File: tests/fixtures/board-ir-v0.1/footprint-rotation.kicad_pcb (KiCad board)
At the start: 2 copper layers, 44 x 40 mm, 8 parts

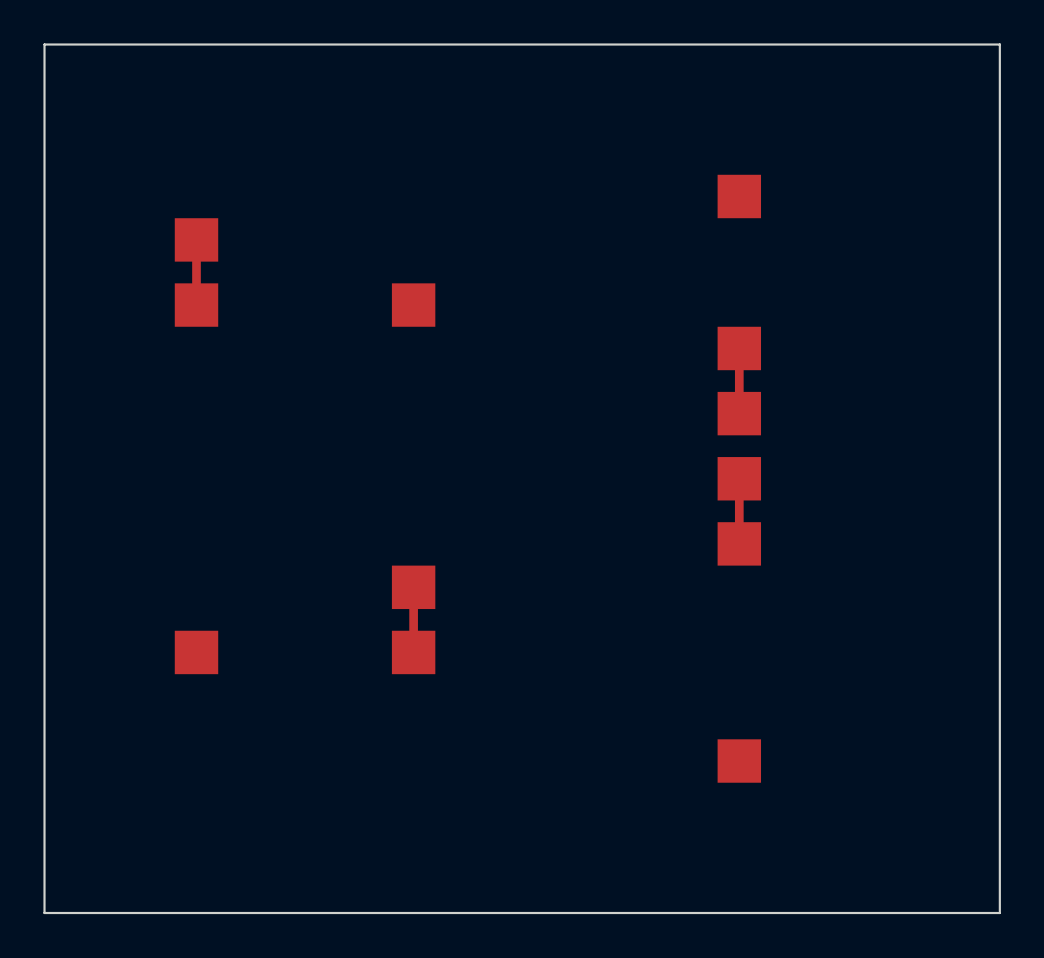
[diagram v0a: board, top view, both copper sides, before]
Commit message: fix: rotate pads absolutely and close six scene observation gaps (#41)
KiCad pad angles are absolute in the board frame, so the adapter's
addition of the footprint rotation double-counted every rotated pad and
transposed extents on non-square pads; the fix is pinned by the first
adapter test adjudicated by an external oracle, comparing Board IR
extents against the geometry KiCad itself plots, mutation-tested by
reinstating the defect. On the reference board different-net bbox
overlaps fall from six to one, the survivor being a corner both real
shapes round away, and no route outcome changes. The scene closes its
review findings: annotations are budgeted with explicit truncation,
region bounds include the arc extrema a sweep actually crosses under a
magnitude-independent exact comparator verified over four hundred
random arcs, oblique pads fall back to the circumscribed circle rather
than under-bounding, locked copper carries a per-object flag while the
partition stays exhaustive by kind, roundrect corner radii reach the
contract, and around-reference radii clamp losslessly instead of
overflowing. Golden fixture changes are exactly two pad rotations plus
the digest, diffed field by field before regeneration.

Co-authored-by: Seung Hyuk Choe <10142803+seunghyukchoe@users.noreply.github.com>
Co-authored-by: Claude Fable 5 <noreply@anthropic.com>
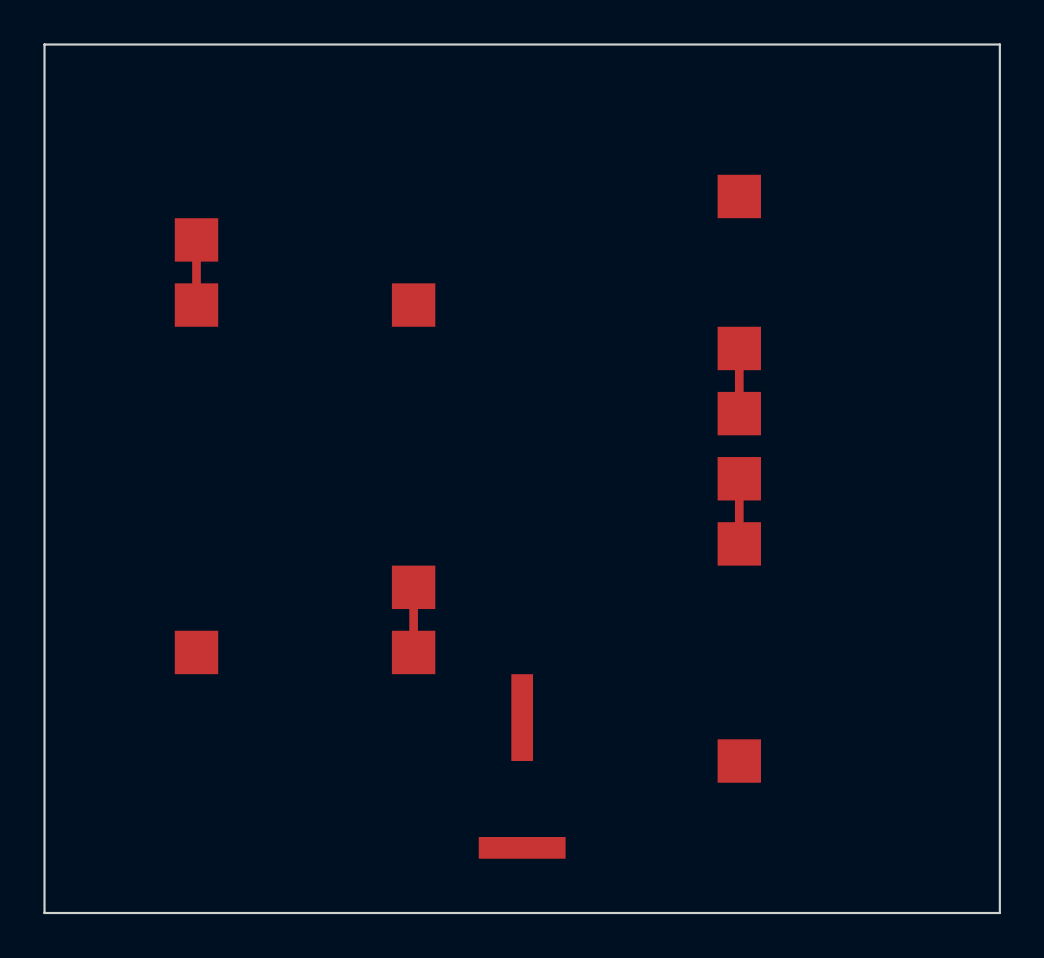
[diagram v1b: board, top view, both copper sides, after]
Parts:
- added ?: , RotationOblong_90, F.Cu at (22.0, 34.0)
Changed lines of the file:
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@@
     (at 32 12 90)
     (pad "1" smd rect
-      (at -5 0)
+      (at -5 0 90)
       (size 2 2)
       (layers "F.Cu" "F.Mask" "F.Paste")
@@
     )
     (pad "2" smd rect
-      (at 5 0)
+      (at 5 0 90)
       (size 2 2)
       (layers "F.Cu" "F.Mask" "F.Paste")
@@
     (at 12 28 180)
     (pad "1" smd rect
-      (at -5 0)
+      (at -5 0 180)
       (size 2 2)
       (layers "F.Cu" "F.Mask" "F.Paste")
@@
     )
     (pad "2" smd rect
-      (at 5 0)
+      (at 5 0 180)
       (size 2 2)
       (layers "F.Cu" "F.Mask" "F.Paste")
@@
     (at 32 28 270)
     (pad "1" smd rect
-      (at -5 0)
+      (at -5 0 270)
       (size 2 2)
       (layers "F.Cu" "F.Mask" "F.Paste")
@@
     )
     (pad "2" smd rect
-      (at 5 0)
+      (at 5 0 270)
       (size 2 2)
       (layers "F.Cu" "F.Mask" "F.Paste")
@@
     (net "PROBE_270_A")
   )
+  (footprint "RotationOblong_90"
+    (layer "F.Cu")
+    (at 22 34 90)
+    (pad "1" smd rect
+      (at 3 0 90)
+      (size 4 1)
+      (layers "F.Cu" "F.Mask" "F.Paste")
+      (net "OBLONG_ROT")
+    )
+    (pad "2" smd rect
+      (at -3 0 0)
+      (size 4 1)
+      (layers "F.Cu" "F.Mask" "F.Paste")
+      (net "OBLONG_FIX")
+    )
+  )
   (gr_rect
